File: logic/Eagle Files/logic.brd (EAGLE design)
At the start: 86 x 80.5 mm, 78 parts, among them J1 Under Glow, J2 B2PS-VH(LF)(SN), J3 B2PS-VH(LF)(SN), J4 B2PS-VH(LF)(SN), J5 B2PS-VH(LF)(SN), J6 B2PS-VH(LF)(SN), Q4 STT4P3LLH6, Q5 RRH100P03GZETB, T1 R-78E5.0-1.0, U1 9DoF IMU, U4 TLV70233DBVR, U5 TC4427ACOA713, U6 TC4427ACOA713, U7 TC4427ACOA713, X1 MINI-USB_SHIELD5P4-32005-400, X2 C-GRID-05-15-91, X3 2510-, X4 2510-, X5 C-GRID-05-15-91, X6 C-GRID-02-70553, X7 SI-50170

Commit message: added various components
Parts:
- added C11: 0.1uF, rcl:C0603
- added C12: 1nF, rcl:C0603
- added R2: 1k, rcl:R0603
- added U$17: ACS711, IGVC-Sensor:POWERPAK_8X8L
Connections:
- new net N$3: C12.1, U$17.P$7
- new net N$4: R2.1, U$17.P$1
- new net N$5: U$17.P$10
- new net N$6: U$17.P$9
- net +3V3: now also C11.1, R2.2, U$17.P$8
- net GND: now also C11.2, C12.2, U$17.P$2

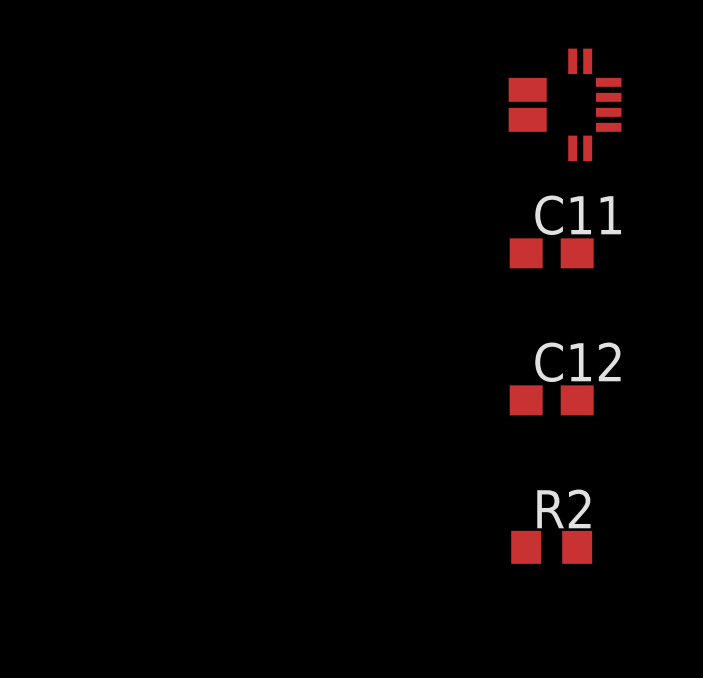
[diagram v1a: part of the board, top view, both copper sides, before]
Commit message: added safety light power
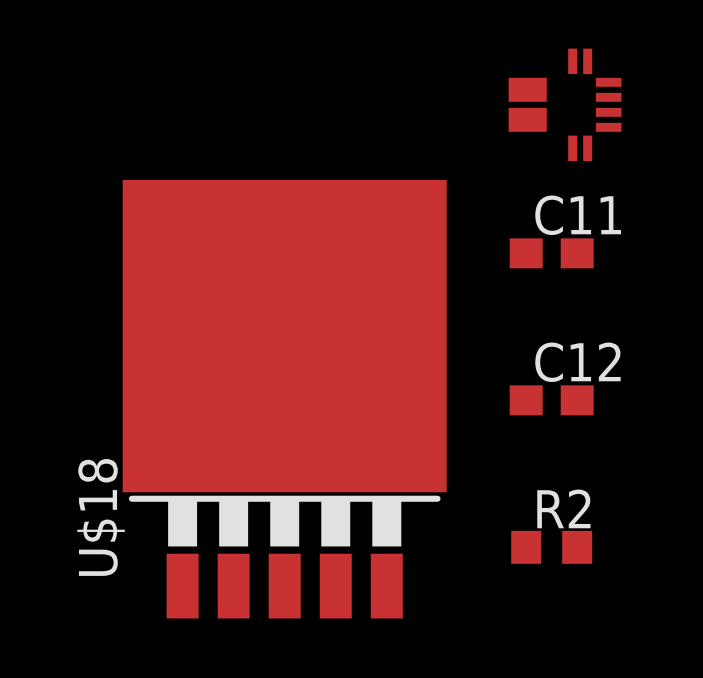
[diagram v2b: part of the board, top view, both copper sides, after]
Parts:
- added U$18: MIS29301-12, IGVC-Regulator:TO263-5
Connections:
- net N$6 renamed +12V_SAFETY_LIGHT
- removed net N$5: U$17.P$10
- new net +12V_SAFETY_CURRSENSE: U$17.P$10, U$18.4
- new net SAFETY_LIGHT_EN: U$18.1
- new net SAFETY_LIGHT_FLG: U$18.5
- net +12V: now also U$18.2
- net GND: now also U$18.3, U$18.6
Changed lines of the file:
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@@
 <attribute name="SPICEPREFIX" value="R" x="1.5" y="-22.6" size="1.778" layer="27" display="off"/>
 </element>
+<element name="U$18" library="IGVC-Regulator" package="TO263-5" value="MIS29301-12" x="-7.4" y="-18.1"/>
 </elements>
 <signals>
@@
 <contactref element="C12" pad="2"/>
 <contactref element="U$17" pad="P$2"/>
+<contactref element="U$18" pad="6"/>
+<contactref element="U$18" pad="3"/>
 <wire x1="75.3" y1="77.25" x2="79.25" y2="75.812" width="0" layer="19" extent="16-16"/>
 <wire x1="69.7" y1="77.25" x2="75.3" y2="77.25" width="0" layer="19" extent="16-16"/>
@@
 <wire x1="2.35" y1="-12.8" x2="2.2" y2="-9.3" width="0" layer="19" extent="1-1"/>
 <wire x1="2.35" y1="-17.7" x2="2.35" y2="-12.8" width="0" layer="19" extent="1-1"/>
+<wire x1="-7.4" y1="-15.56" x2="2.35" y2="-17.7" width="0" layer="19" extent="1-1"/>
+<wire x1="-7.4" y1="-23.8912" x2="-7.4" y2="-15.56" width="0" layer="19" extent="1-1"/>
 </signal>
 <signal name="SDA">
@@
 <contactref element="U6" pad="6"/>
 <contactref element="U7" pad="6"/>
+<contactref element="U$18" pad="2"/>
+<wire x1="8.65" y1="57.42" x2="5.8" y2="67.55" width="0" layer="19" extent="1-1"/>
+<wire x1="14.25" y1="56.3" x2="8.65" y2="57.42" width="0" layer="19" extent="1-1"/>
+<wire x1="11.0766" y1="50.185" x2="14.25" y2="56.3" width="0" layer="19" extent="1-1"/>
+<wire x1="11.0766" y1="43.735" x2="11.0766" y2="50.185" width="0" layer="19" extent="1-1"/>
+<wire x1="11.0766" y1="37.385" x2="11.0766" y2="43.735" width="0" layer="19" extent="1-1"/>
+<wire x1="27" y1="36.51" x2="11.0766" y2="37.385" width="0" layer="19" extent="1-1"/>
+<wire x1="28.35" y1="31.1" x2="27" y2="36.51" width="0" layer="19" extent="1-1"/>
+<wire x1="17.455" y1="12.1734" x2="28.35" y2="31.1" width="0" layer="19" extent="1-1"/>
+<wire x1="-9.1018" y1="-23.8912" x2="14.915" y2="12.1734" width="0" layer="19" extent="1-1"/>
 </signal>
 <signal name="SAFETY_HRD">
@@
 <wire x1="2.7" y1="-9.3" x2="0.65" y2="-22.6" width="0" layer="19" extent="1-1"/>
 </signal>
-<signal name="N$5">
+<signal name="+12V_SAFETY_LIGHT">
+<contactref element="U$17" pad="P$9"/>
+</signal>
+<signal name="+12V_SAFETY_CURRSENSE">
+<contactref element="U$18" pad="4"/>
 <contactref element="U$17" pad="P$10"/>
-</signal>
-<signal name="N$6">
-<contactref element="U$17" pad="P$9"/>
+<wire x1="0.7" y1="-7.35" x2="-5.6982" y2="-23.8912" width="0" layer="19" extent="1-1"/>
+</signal>
+<signal name="SAFETY_LIGHT_EN">
+<contactref element="U$18" pad="1"/>
+</signal>
+<signal name="SAFETY_LIGHT_FLG">
+<contactref element="U$18" pad="5"/>
 </signal>
 </signals>

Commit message: fixed +24V to safety regulator
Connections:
- net +12V: no longer U$18.2
- net +24V: now also U$18.2
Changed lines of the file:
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@@
 <contactref element="U6" pad="6"/>
 <contactref element="U7" pad="6"/>
-<contactref element="U$18" pad="2"/>
 <wire x1="8.65" y1="57.42" x2="5.8" y2="67.55" width="0" layer="19" extent="1-1"/>
 <wire x1="14.25" y1="56.3" x2="8.65" y2="57.42" width="0" layer="19" extent="1-1"/>
@@
 <wire x1="28.35" y1="31.1" x2="27" y2="36.51" width="0" layer="19" extent="1-1"/>
 <wire x1="17.455" y1="12.1734" x2="28.35" y2="31.1" width="0" layer="19" extent="1-1"/>
-<wire x1="-9.1018" y1="-23.8912" x2="14.915" y2="12.1734" width="0" layer="19" extent="1-1"/>
 </signal>
 <signal name="SAFETY_HRD">
@@
 <wire x1="15.35" y1="18.7" x2="20.15" y2="18.7" width="0.5" layer="1"/>
 <wire x1="20.15" y1="18.7" x2="21.2" y2="17.65" width="0.5" layer="1"/>
+<contactref element="U$18" pad="2"/>
+<wire x1="8.15" y1="15.32" x2="-9.1018" y2="-23.8912" width="0" layer="19" extent="1-1"/>
 </signal>
 <signal name="24V_LED_R">

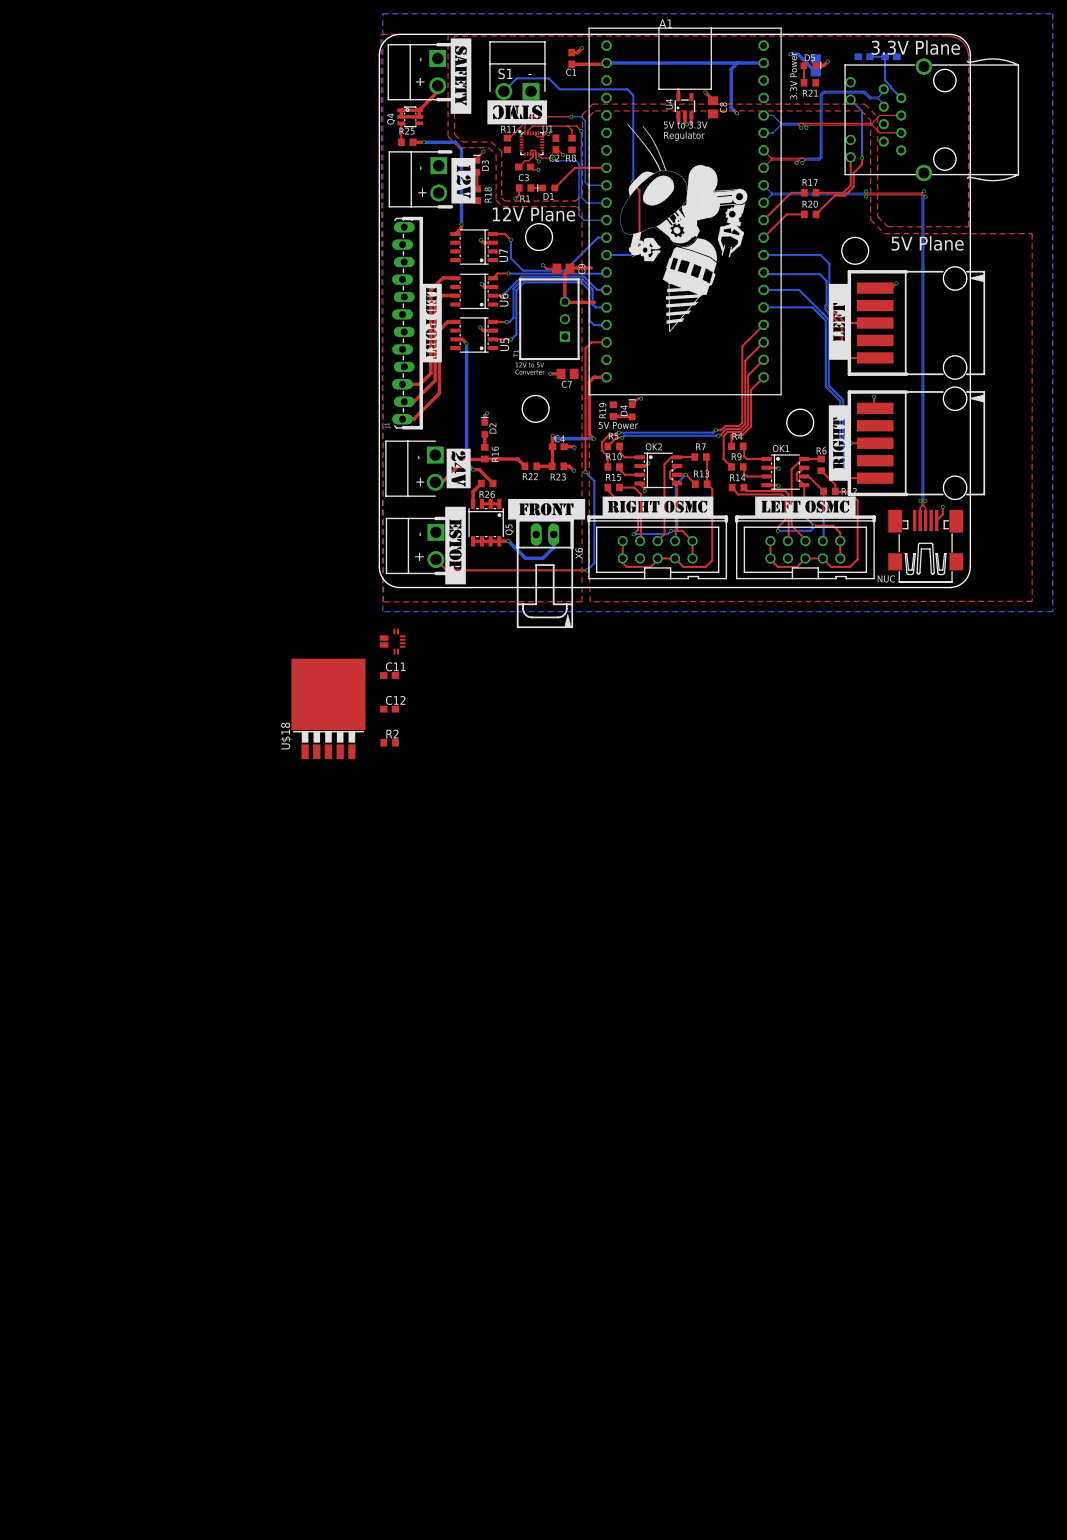
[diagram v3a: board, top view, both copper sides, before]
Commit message: added more power and removed old circuits
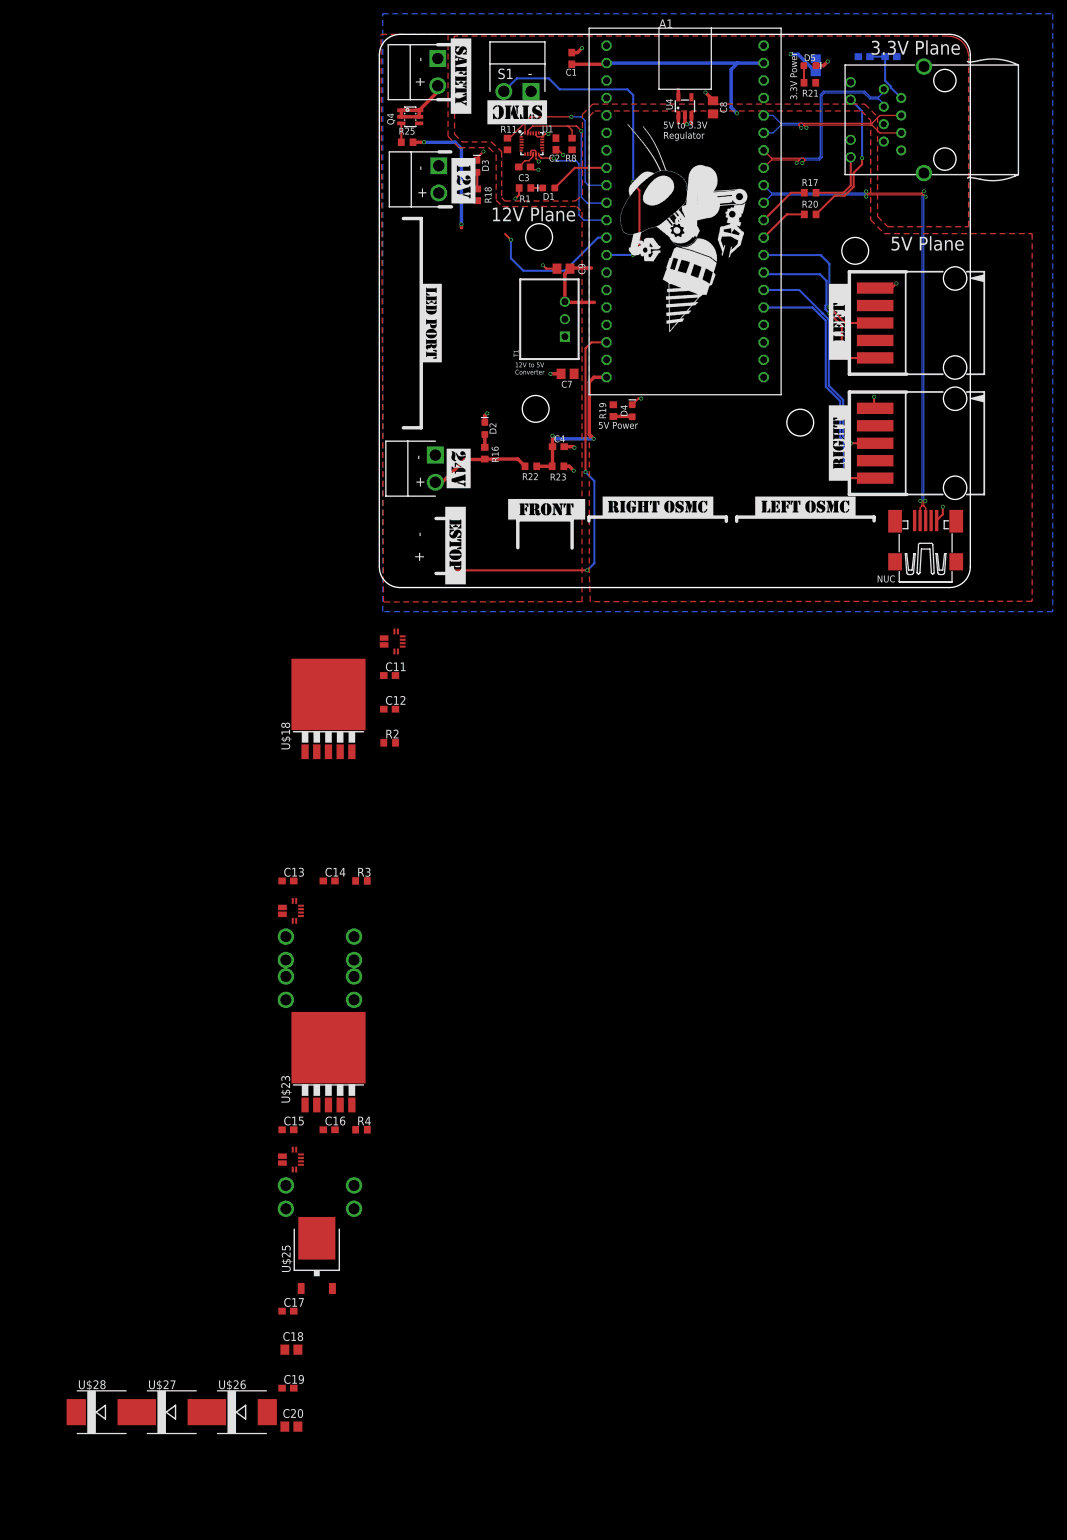
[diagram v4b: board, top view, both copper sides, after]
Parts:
- removed J1: Under Glow, SparkFun-Connectors:1X12_LOCK_LONGPADS
- removed J5: B2PS-VH(LF)(SN), RoboJackets-Connectors:B2PS-CENTERED
- removed OK1, OK2: MOCD208M, optocoupler:SOIC08-FAIRCHILD
- removed Q5: RRH100P03GZETB, MotorBoardDev:SOIC-8
- removed R10, R5, R9: 30, rcl:R0603
- removed R12, R13, R6, R7: 4.7k, rcl:R0603
- removed R14, R15: 1k, rcl:R0603
- removed R26: 2.7k, rcl:R0603
- removed U5, U6, U7: TC4427ACOA713, MotorBoardDev:SOIC-8
- removed X3, X4: 2510-, con-3m:PAK100/2500-10
- removed X6: C-GRID-02-70553, con-molex:70553-02
- added C13, C15, C17, C19: 0.1uF, rcl:C0603
- added C14, C16: 1nF, rcl:C0603
- added C18, C20: 10uF, rcl:C0805
- added R3: 1k, rcl:R0603
- added U$19, U$22: ACS711, IGVC-Sensor:POWERPAK_8X8L
- added U$20, U$21, U$24: FUSE_HOLDER, IGVC-Misc:FUSE_HOLDER
- added U$23: MIS29301-12, IGVC-Regulator:TO263-5
- added U$25: BUK9226, IGVC-Discrete:DPACK
- added U$26, U$27, U$28: S10M-TP, IGVC-Discrete:SMC
- R4: value 30 -> 1k
- moved R4 113.5 mm to (-2.60, -78.9)
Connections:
- removed net BLUE_3V3: A1.16, U5.4
- removed net BLUE_OUT: J1.1, U5.5
- removed net FRONT_HDR: Q5.5, Q5.6, Q5.7, Q5.8, X6.1
- removed net FRONT_LIGHT: R26.1, U5.7
- removed net FRONT_LIGHT_3V3: A1.17, U5.2
- removed net FRONT_R: Q5.4, R26.2
- removed net GREEN_3V3: A1.15, U6.2
- removed net GREEN_OUT: J1.2, U6.7
- removed net L+12V: R12.2, R6.2, X3.1, X3.2, X3.5, X3.7
- removed net LALI: OK1.8, R6.1, X3.6
- removed net LALI_CTRL: A1.21, R4.1
- removed net LBLI: OK1.6, R12.1, X3.8
- removed net LBLI_CTRL: A1.22, R9.1
- removed net LDISABLE: R14.2, X3.4
- removed net LGND: OK1.5, OK1.7, R14.1, X3.10, X3.9
- removed net R+12V: R13.2, R7.2, X4.1, X4.2, X4.5, X4.7
- removed net RALI: OK2.8, R7.1, X4.6
- removed net RALI_CTRL: A1.23, R5.1
- removed net RBLI: OK2.6, R13.1, X4.8
- removed net RBLI_CTRL: A1.24, R10.1
- removed net RDISABLE: R15.2, X4.4
- removed net RED_3V3: A1.14, U6.4
- removed net RED_OUT: J1.3, U6.5
- removed net RGND: OK2.5, OK2.7, R15.1, X4.10, X4.9
- removed net R_OK3A: OK1.1, R4.2
- removed net R_OK3B: OK1.3, R9.2
- removed net R_OK4A: OK2.1, R5.2
- removed net R_OK4B: OK2.3, R10.2
- new net +12V_FAN: U$22.P$9
- new net +12V_FAN_CURRSENSE: U$22.P$10, U$24.P$3, U$24.P$4
- new net +12V_FAN_FUSE: C18.1, U$23.4, U$24.P$1, U$24.P$2
- new net +12V_SAFETY_FUSE: C20.1, U$18.4, U$20.P$1, U$20.P$2
- new net +24V_FLOOD_CURRSENSE: U$19.P$10, U$21.P$3, U$21.P$4
- new net +24V_FLOOD_FUSE: U$21.P$1, U$21.P$2, U$25.3
- new net +24V_FLOOD_LIGHT: U$19.P$9
- new net DIODE_TO_INTER: U$27.C
- new net DIODE_TO_RED: U$26.C
- new net FAN_EN: U$23.1
- new net FAN_FLG: U$23.5
- new net FLOOD_LIGHT_EN: U$25.1
- new net N$5: C14.1, U$19.P$7
- new net N$6: R3.1, U$19.P$1
- new net N$7: C16.1, U$22.P$7
- new net N$8: R4.1, U$22.P$1
- new net SOLENOID_TO_DIODE: U$27.A
- new net SOLENOID_TRIG: U$28.C
- new net SOLENOID_TRIG_GND: U$28.A
- net +12V: no longer Q5.1, Q5.2, Q5.3, U5.6, U6.6, U7.6
- net +12V_SAFETY_CURRSENSE: now also U$20.P$3, U$20.P$4; no longer U$18.4
- net +24V: now also C17.1, C19.1, U$23.2, U$25.2, U$26.A
- net +3V3: now also C13.1, C15.1, R3.2, R4.2, U$19.P$8, U$22.P$8
- net ESTOP: no longer J5.2
- net GND: now also C13.2, C14.2, C15.2, C16.2, C17.2, C18.2, C19.2, C20.2, U$19.P$2, U$22.P$2, U$23.3, U$23.6; no longer J1.10, J1.11, J1.12, J1.4, J1.5, J1.6, J5.1, OK1.2, OK1.4, OK2.2, OK2.4, U5.3, U6.3, U7.3, X6.2
- net SAFETY_LIGHT: no longer U7.5
- net SAFETY_LIGHT_3V3: no longer U7.4
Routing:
- net RBLI_CTRL: track 41.0 -> 0.00 mm, vias 2 -> 0
- net LGND: track 38.2 -> 0.00 mm, vias 2 -> 0
- net RALI_CTRL: track 34.3 -> 0.00 mm, vias 2 -> 0
- net L+12V: track 33.5 -> 0.00 mm
- net R+12V: track 33.5 -> 0.00 mm
- net RGND: track 33.0 -> 0.00 mm, vias 2 -> 0
- net FRONT_LIGHT_3V3: track 28.9 -> 0.00 mm, vias 1 -> 0
- net BLUE_3V3: track 24.6 -> 0.00 mm, vias 1 -> 0
- net FRONT_LIGHT: track 24.4 -> 0.00 mm, vias 2 -> 0
- net RED_OUT: track 21.8 -> 0.00 mm
- net GREEN_OUT: track 20.5 -> 0.00 mm
- net LBLI_CTRL: track 19.7 -> 0.00 mm
- net BLUE_OUT: track 19.0 -> 0.00 mm
- net GREEN_3V3: track 18.5 -> 0.00 mm, vias 1 -> 0
- net RED_3V3: track 16.9 -> 0.00 mm, vias 1 -> 0
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
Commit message: added new imu
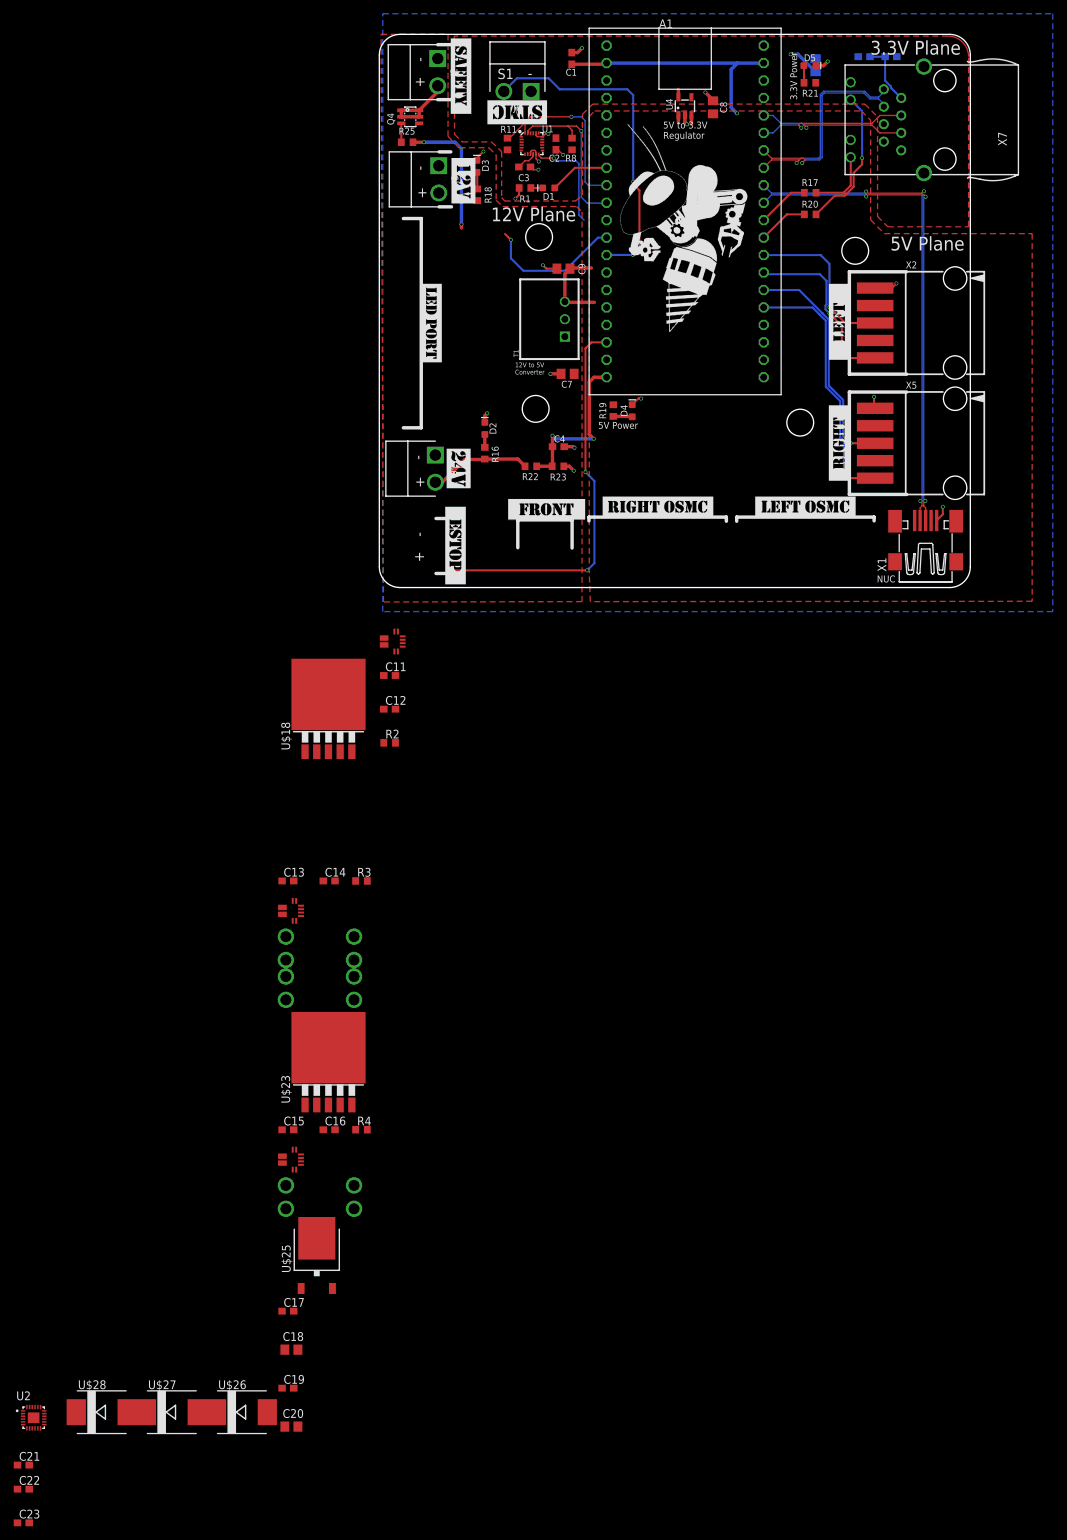
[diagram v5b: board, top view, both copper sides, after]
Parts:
- added C21, C22, C23: 0.1uF, rcl:C0603
- added U2: ICM-20948, ICM-20948:QFN40P300X300X105-25N
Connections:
- new net +1V8: C22.1, U2.22, U2.8
- new net IMU_INT: A1.11, U2.12
- new net N$9: C23.1, U2.10
- net +3V3: now also C21.1, U2.13
- net GND: now also C21.2, C22.2, C23.2, U2.11, U2.18, U2.20, U2.25, U2.9
- net GYRO_INT: no longer A1.11
- net SCL: now also U2.23
- net SDA: now also U2.24
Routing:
- net GYRO_INT: track 18.3 -> 15.0 mm
